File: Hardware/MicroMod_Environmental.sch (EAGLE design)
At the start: 26 parts, among them J1 MICROMOD_STANDARD, U1 SGP40, U3 SHTC3, U4 3.3V, U5 STC31

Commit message: Routed
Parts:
- added U2: EEPROM, SparkFun-IC-Memory:EEPROM-I2C512K
- C5, C6: device SparkFun-Capacitors:1.0UF-0402T-16V-10% -> SparkFun-Capacitors:1.0UF-0603-16V-10%
- R12: value 100K -> 100k; device SparkFun-Resistors:100KOHM-0402-1/16W-1% -> SparkFun-Resistors:100KOHM-0603-1/10W-1%
- R3: device SparkFun-Resistors:1KOHM-0402T-1/16W-1% -> SparkFun-Resistors:1KOHM-0603-1/10W-1%
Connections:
- removed net GND1: LED2.C
- new net A0: J1.EEPROM_A0, U2.A0
- new net A1: J1.EEPROM_A1, U2.A1
- new net A2: J1.EEPROM_A2, U2.A2
- net 3.3V: now also U2.VCC; no longer J1.3.3V
- net GND: now also LED2.C, U2.GND, U2.WP
- net SCL: now also U2.SCL
- net SDA: now also U2.SDA
- net VCC: now also J1.VCC
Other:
- note added: "EEPROM"
- moved on the sheet: 0X2A, 0X2B, 0X2C, C2, C3, C4, C5, C6, C7, J1, JP1, LED2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

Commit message: Small tweaks to traces
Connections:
- removed net 3.3V1: PWR\.2
- net 3.3V: now also PWR\.2
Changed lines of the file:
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@@
 <wire x1="68.58" y1="76.2" x2="68.58" y2="78.74" width="0.1524" layer="91"/>
+</segment>
+<segment>
+<wire x1="142.24" y1="190.5" x2="139.7" y2="190.5" width="0.1524" layer="91"/>
+<pinref part="PWR\" gate="G$1" pin="2"/>
+<pinref part="SUPPLY12" gate="G$1" pin="3.3V"/>
+<wire x1="139.7" y1="190.5" x2="139.7" y2="200.66" width="0.1524" layer="91"/>
 </segment>
 </net>
@@
 </segment>
 </net>
-<net name="3.3V1" class="2">
-<segment>
-<wire x1="142.24" y1="190.5" x2="139.7" y2="190.5" width="0.1524" layer="91"/>
-<wire x1="139.7" y1="200.66" x2="139.7" y2="190.5" width="0.1524" layer="91"/>
-<pinref part="PWR\" gate="G$1" pin="2"/>
-<pinref part="SUPPLY12" gate="G$1" pin="3.3V"/>
-</segment>
-</net>

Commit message: Adds silk, fiducials, and version number
* Adds text to part boxes in schematic
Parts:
- added FD1, FD2, FD3, FD4: FIDUCIAL1X2, SparkFun-Aesthetics:FIDUCIAL1X2
- added LOGO1: SFE_LOGO_NAME_FLAME.2_INCH, SparkFun-Aesthetics:SFE_LOGO_NAME_FLAME.2_INCH
- added LOGO2: OSHW-LOGOS, SparkFun-Aesthetics:OSHW-LOGOS
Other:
- note added: "Air Quality Sensor: SGP40"
- note added: "CO2 Sensor: STC31"
- note added: "Function Connector"
- note added: "Humidity and Temperature: SHTC3"
- note added: "Jumpers"
- note added: "Voltage Regulation"
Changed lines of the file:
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@@
 <part name="SUPPLY13" library="SparkFun-PowerSymbols" deviceset="VCC" device=""/>
 <part name="GND10" library="SparkFun-PowerSymbols" deviceset="GND" device=""/>
+<part name="LOGO1" library="SparkFun-Aesthetics" deviceset="SFE_LOGO_NAME_FLAME" device=".2_INCH" value="SFE_LOGO_NAME_FLAME.2_INCH"/>
+<part name="LOGO2" library="SparkFun-Aesthetics" deviceset="OSHW-LOGO" device="S"/>
+<part name="FD1" library="SparkFun-Aesthetics" deviceset="FIDUCIAL" device="1X2"/>
+<part name="FD2" library="SparkFun-Aesthetics" deviceset="FIDUCIAL" device="1X2"/>
+<part name="FD3" library="SparkFun-Aesthetics" deviceset="FIDUCIAL" device="1X2"/>
+<part name="FD4" library="SparkFun-Aesthetics" deviceset="FIDUCIAL" device="1X2"/>
 </parts>
 <sheets>
@@
 <wire x1="111.76" y1="160.02" x2="223.52" y2="160.02" width="0.1524" layer="97" style="longdash"/>
 <wire x1="111.76" y1="279.4" x2="111.76" y2="160.02" width="0.1524" layer="97" style="longdash"/>
+<text x="38.1" y="269.24" size="2.54" layer="94" font="vector">Voltage Regulation</text>
+<text x="154.94" y="271.78" size="2.54" layer="94" font="vector">Jumpers</text>
+<text x="297.18" y="271.78" size="2.54" layer="94" font="vector">Humidity and Temperature: SHTC3</text>
+<text x="309.88" y="195.58" size="2.54" layer="94" font="vector">CO2 Sensor: STC31</text>
+<text x="96.52" y="149.86" size="2.54" layer="94" font="vector">Function Connector</text>
+<text x="309.88" y="109.22" size="2.54" layer="94" font="vector">Air Quality Sensor: SGP40</text>
 </plain>
 <instances>
@@
 <attribute name="VALUE" x="180.34" y="182.88" size="1.778" layer="96" font="vector"/>
 </instance>
+<instance part="LOGO1" gate="G$1" x="330.2" y="35.56" smashed="yes"/>
+<instance part="LOGO2" gate="G$1" x="401.32" y="48.26" smashed="yes"/>
+<instance part="FD1" gate="G$1" x="421.64" y="33.02" smashed="yes"/>
+<instance part="FD2" gate="G$1" x="419.1" y="30.48" smashed="yes"/>
+<instance part="FD3" gate="G$1" x="419.1" y="33.02" smashed="yes"/>
+<instance part="FD4" gate="G$1" x="421.64" y="30.48" smashed="yes"/>
 </instances>
 <busses>

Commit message: Reroutes board
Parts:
- renumbered LED2 to LED1
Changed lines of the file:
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@@
 <part name="SUPPLY7" library="SparkFun-PowerSymbols" deviceset="VCC" device=""/>
 <part name="R3" library="SparkFun-Resistors" deviceset="1KOHM" device="-0603-1/10W-1%" value="1k"/>
-<part name="LED2" library="SparkFun-LED" deviceset="LED-RED" device="0603" value="RED"/>
+<part name="LED1" library="SparkFun-LED" deviceset="LED-RED" device="0603" value="RED"/>
 <part name="PWR\" library="SparkFun-Jumpers" deviceset="JUMPER-SMT_2_NC_TRACE" device="_SILK" package3d_urn="urn:adsk.eagle:package:39281/1" value="JUMPER-SMT_2_NC_TRACE_SILK"/>
 <part name="SUPPLY12" library="SparkFun-PowerSymbols" deviceset="3.3V" device=""/>
@@
 <attribute name="VALUE" x="155.448" y="191.008" size="1.778" layer="96" font="vector" rot="R180" align="top-center"/>
 </instance>
-<instance part="LED2" gate="G$1" x="170.18" y="190.5" smashed="yes" rot="R90">
+<instance part="LED1" gate="G$1" x="170.18" y="190.5" smashed="yes" rot="R90">
 <attribute name="NAME" x="179.832" y="190.119" size="1.778" layer="95" font="vector" rot="R180"/>
 <attribute name="VALUE" x="178.308" y="191.008" size="1.778" layer="96" font="vector" rot="R180" align="top-left"/>
@@
 <wire x1="182.88" y1="190.5" x2="175.26" y2="190.5" width="0.1524" layer="91"/>
 <wire x1="182.88" y1="190.5" x2="182.88" y2="187.96" width="0.1524" layer="91"/>
-<pinref part="LED2" gate="G$1" pin="C"/>
+<pinref part="LED1" gate="G$1" pin="C"/>
 <pinref part="GND10" gate="1" pin="GND"/>
 </segment>
@@
 <wire x1="167.64" y1="190.5" x2="165.1" y2="190.5" width="0.1524" layer="91"/>
 <pinref part="R3" gate="G$1" pin="1"/>
-<pinref part="LED2" gate="G$1" pin="A"/>
+<pinref part="LED1" gate="G$1" pin="A"/>
 </segment>
 </net>

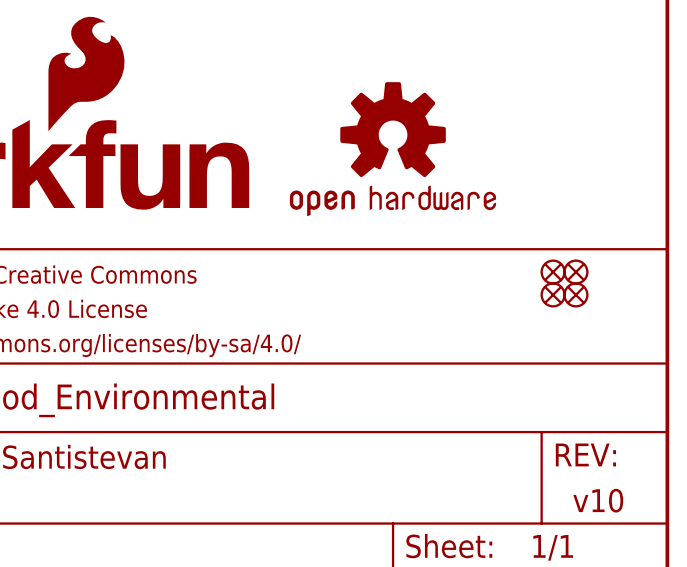
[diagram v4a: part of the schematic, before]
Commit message: Adds address table in silk, adds a more symmetrical cutout around IC's, labels ICs in silk
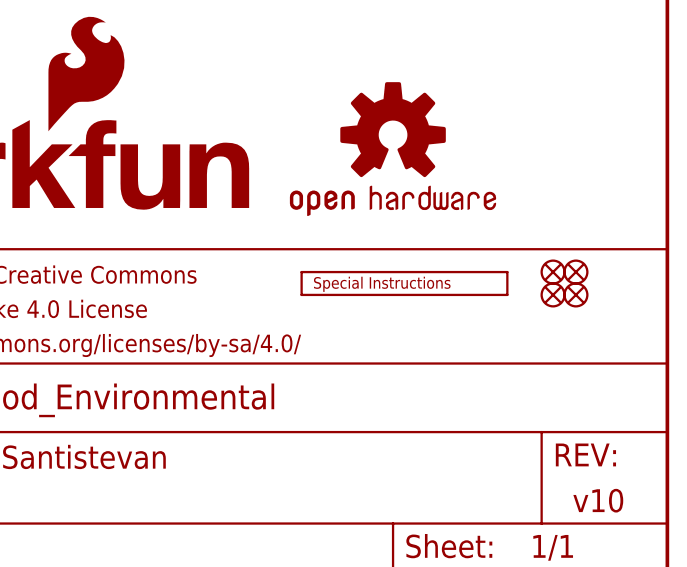
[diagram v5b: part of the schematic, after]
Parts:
- added LOGO3: SPECIAL_INSTRUCTIONS-ORDERING, SparkFun-Aesthetics:SPECIAL_INSTRUCTIONS-ORDERING
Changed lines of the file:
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@@
 <part name="FD3" library="SparkFun-Aesthetics" deviceset="FIDUCIAL" device="1X2"/>
 <part name="FD4" library="SparkFun-Aesthetics" deviceset="FIDUCIAL" device="1X2"/>
+<part name="LOGO3" library="SparkFun-Aesthetics" deviceset="SPECIAL_INSTRUCTIONS" device="-ORDERING"/>
 </parts>
 <sheets>
@@
 <instance part="FD3" gate="G$1" x="419.1" y="33.02" smashed="yes"/>
 <instance part="FD4" gate="G$1" x="421.64" y="30.48" smashed="yes"/>
+<instance part="LOGO3" gate="G$1" x="391.16" y="30.48" smashed="yes"/>
 </instances>
 <busses>

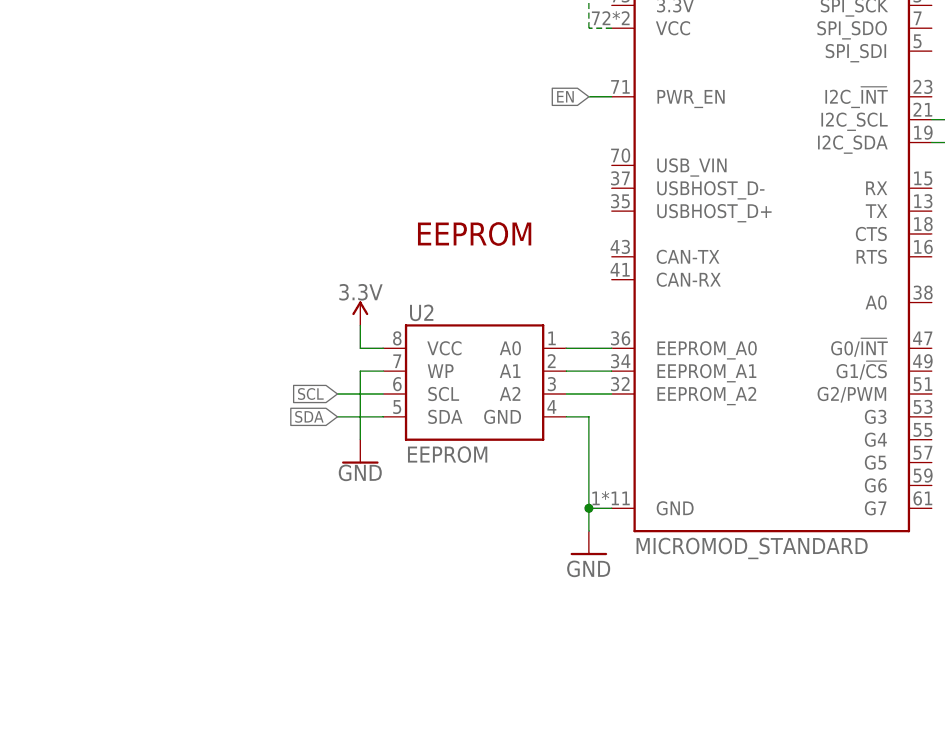
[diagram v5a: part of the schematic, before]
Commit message: Adds pullup and jumper to the EEPROM's write protect, brings WP pin to card's edge
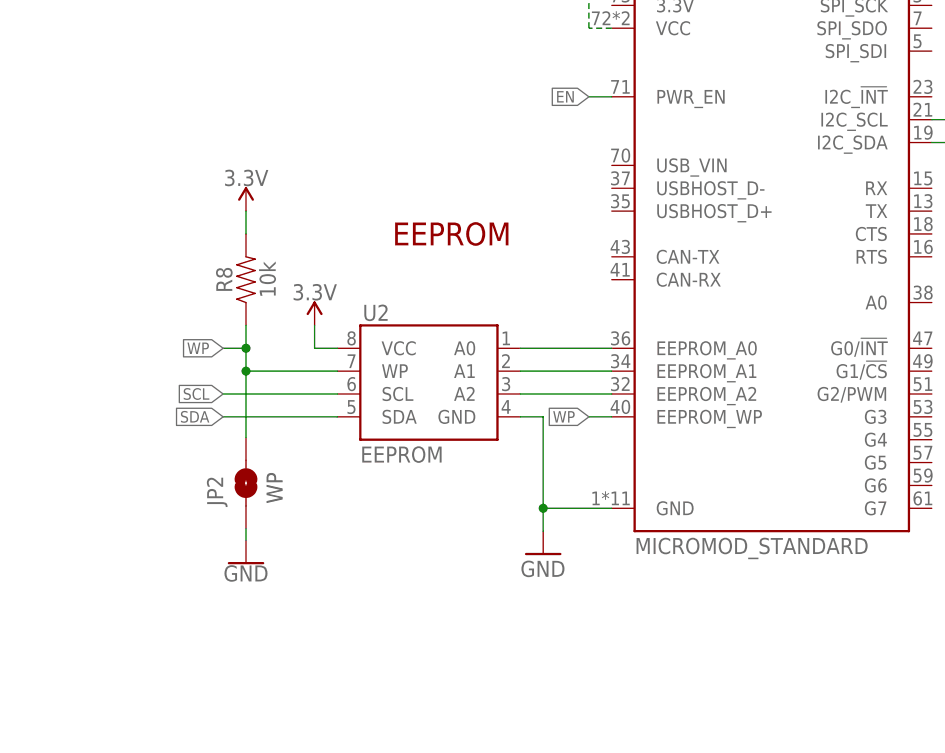
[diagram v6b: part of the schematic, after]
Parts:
- added JP2: JUMPER-SMT_2_NO_SILK, SparkFun-Jumpers:JUMPER-SMT_2_NO_SILK
- added R8: 10k, SparkFun-Resistors:10KOHM-0603-1/10W-1%
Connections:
- new net WP: J1.EEPROM_WP, JP2.2, R8.1, U2.WP
- net 3.3V: now also R8.2
- net GND: now also JP2.1; no longer U2.WP
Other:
- note added: "WP"
- moved on the sheet: U2
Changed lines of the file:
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@@
 <part name="FD4" library="SparkFun-Aesthetics" deviceset="FIDUCIAL" device="1X2"/>
 <part name="LOGO3" library="SparkFun-Aesthetics" deviceset="SPECIAL_INSTRUCTIONS" device="-ORDERING"/>
+<part name="SUPPLY15" library="SparkFun-PowerSymbols" deviceset="3.3V" device=""/>
+<part name="R8" library="SparkFun-Resistors" deviceset="10KOHM" device="-0603-1/10W-1%" value="10k"/>
+<part name="JP2" library="SparkFun-Jumpers" deviceset="JUMPER-SMT_2_NO" device="_SILK" package3d_urn="urn:adsk.eagle:package:39279/1"/>
 </parts>
 <sheets>
@@
 <text x="297.18" y="53.34" size="1.778" layer="97" font="vector" align="center">Abs min/max Vdd and Vddh: -0.3 to +3.6V
 Operating current @ 3.3V: 3.0 mA</text>
-<text x="81.28" y="88.9" size="2.54" layer="94" font="vector" align="center">EEPROM</text>
+<text x="78.74" y="88.9" size="2.54" layer="94" font="vector" align="center">EEPROM</text>
 <wire x1="223.52" y1="279.4" x2="223.52" y2="205.74" width="0.1524" layer="97" style="longdash"/>
 <wire x1="223.52" y1="205.74" x2="223.52" y2="160.02" width="0.1524" layer="97" style="longdash"/>
@@
 <text x="96.52" y="149.86" size="2.54" layer="94" font="vector">Function Connector</text>
 <text x="309.88" y="109.22" size="2.54" layer="94" font="vector">Air Quality Sensor: SGP40</text>
+<text x="59.944" y="58.928" size="1.778" layer="97" font="vector" rot="R90">WP</text>
 </plain>
 <instances>
@@
 <attribute name="NAME" x="157.226" y="243.205" size="1.778" layer="95" font="vector"/>
 </instance>
-<instance part="GND8" gate="1" x="93.98" y="53.34" smashed="yes">
-<attribute name="VALUE" x="91.44" y="50.8" size="1.778" layer="96" font="vector"/>
-</instance>
-<instance part="U2" gate="G$1" x="81.28" y="71.12" smashed="yes" rot="MR0">
-<attribute name="NAME" x="73.914" y="79.248" size="1.778" layer="95"/>
-<attribute name="VALUE" x="73.66" y="63.5" size="1.778" layer="96"/>
-</instance>
-<instance part="SUPPLY14" gate="G$1" x="68.58" y="78.74" smashed="yes">
-<attribute name="VALUE" x="68.58" y="81.534" size="1.778" layer="96" align="bottom-center"/>
-</instance>
-<instance part="GND9" gate="1" x="68.58" y="63.5" smashed="yes">
-<attribute name="VALUE" x="68.58" y="63.246" size="1.778" layer="96" align="top-center"/>
+<instance part="GND8" gate="1" x="88.9" y="53.34" smashed="yes">
+<attribute name="VALUE" x="86.36" y="50.8" size="1.778" layer="96" font="vector"/>
+</instance>
+<instance part="U2" gate="G$1" x="76.2" y="71.12" smashed="yes" rot="MR0">
+<attribute name="NAME" x="68.834" y="79.248" size="1.778" layer="95"/>
+<attribute name="VALUE" x="68.58" y="63.5" size="1.778" layer="96"/>
+</instance>
+<instance part="SUPPLY14" gate="G$1" x="63.5" y="78.74" smashed="yes">
+<attribute name="VALUE" x="63.5" y="81.534" size="1.778" layer="96" align="bottom-center"/>
+</instance>
+<instance part="GND9" gate="1" x="55.88" y="52.324" smashed="yes">
+<attribute name="VALUE" x="55.88" y="52.07" size="1.778" layer="96" align="top-center"/>
 </instance>
 <instance part="SUPPLY13" gate="G$1" x="93.98" y="116.84" smashed="yes">
@@
 <instance part="FD4" gate="G$1" x="421.64" y="30.48" smashed="yes"/>
 <instance part="LOGO3" gate="G$1" x="391.16" y="30.48" smashed="yes"/>
+<instance part="SUPPLY15" gate="G$1" x="55.88" y="91.44" smashed="yes">
+<attribute name="VALUE" x="55.88" y="94.234" size="1.778" layer="96" align="bottom-center"/>
+</instance>
+<instance part="R8" gate="G$1" x="55.88" y="83.82" smashed="yes" rot="R90">
+<attribute name="NAME" x="54.356" y="83.82" size="1.778" layer="95" font="vector" rot="R90" align="bottom-center"/>
+<attribute name="VALUE" x="57.404" y="83.82" size="1.778" layer="96" font="vector" rot="R90" align="top-center"/>
+</instance>
+<instance part="JP2" gate="G$1" x="55.88" y="61.214" smashed="yes" rot="R90">
+<attribute name="NAME" x="53.34" y="58.674" size="1.778" layer="95" font="vector" rot="R90"/>
+</instance>
 </instances>
 <busses>
@@
 <segment>
 <pinref part="U2" gate="G$1" pin="VCC"/>
-<wire x1="71.12" y1="76.2" x2="68.58" y2="76.2" width="0.1524" layer="91"/>
+<wire x1="66.04" y1="76.2" x2="63.5" y2="76.2" width="0.1524" layer="91"/>
 <pinref part="SUPPLY14" gate="G$1" pin="3.3V"/>
-<wire x1="68.58" y1="76.2" x2="68.58" y2="78.74" width="0.1524" layer="91"/>
+<wire x1="63.5" y1="76.2" x2="63.5" y2="78.74" width="0.1524" layer="91"/>
 </segment>
 <segment>
@@
 <pinref part="SUPPLY12" gate="G$1" pin="3.3V"/>
 <wire x1="139.7" y1="190.5" x2="139.7" y2="200.66" width="0.1524" layer="91"/>
+</segment>
+<segment>
+<pinref part="R8" gate="G$1" pin="2"/>
+<pinref part="SUPPLY15" gate="G$1" pin="3.3V"/>
+<wire x1="55.88" y1="88.9" x2="55.88" y2="91.44" width="0.1524" layer="91"/>
 </segment>
 </net>
@@
 <segment>
 <pinref part="J1" gate="J1" pin="GND"/>
-<wire x1="96.52" y1="58.42" x2="93.98" y2="58.42" width="0.1524" layer="91"/>
-<wire x1="93.98" y1="58.42" x2="93.98" y2="55.88" width="0.1524" layer="91"/>
+<wire x1="96.52" y1="58.42" x2="88.9" y2="58.42" width="0.1524" layer="91"/>
+<wire x1="88.9" y1="58.42" x2="88.9" y2="55.88" width="0.1524" layer="91"/>
 <pinref part="GND8" gate="1" pin="GND"/>
 <pinref part="U2" gate="G$1" pin="GND"/>
-<wire x1="91.44" y1="68.58" x2="93.98" y2="68.58" width="0.1524" layer="91"/>
-<wire x1="93.98" y1="68.58" x2="93.98" y2="58.42" width="0.1524" layer="91"/>
-<junction x="93.98" y="58.42"/>
-</segment>
-<segment>
-<pinref part="U2" gate="G$1" pin="WP"/>
-<wire x1="71.12" y1="73.66" x2="68.58" y2="73.66" width="0.1524" layer="91"/>
-<wire x1="68.58" y1="73.66" x2="68.58" y2="66.04" width="0.1524" layer="91"/>
-<pinref part="GND9" gate="1" pin="GND"/>
+<wire x1="86.36" y1="68.58" x2="88.9" y2="68.58" width="0.1524" layer="91"/>
+<wire x1="88.9" y1="68.58" x2="88.9" y2="58.42" width="0.1524" layer="91"/>
+<junction x="88.9" y="58.42"/>
 </segment>
 <segment>
@@
 <pinref part="LED1" gate="G$1" pin="C"/>
 <pinref part="GND10" gate="1" pin="GND"/>
+</segment>
+<segment>
+<pinref part="JP2" gate="G$1" pin="1"/>
+<pinref part="GND9" gate="1" pin="GND"/>
+<wire x1="55.88" y1="56.134" x2="55.88" y2="54.864" width="0.1524" layer="91"/>
 </segment>
 </net>
@@
 <segment>
 <pinref part="U2" gate="G$1" pin="SCL"/>
-<wire x1="71.12" y1="71.12" x2="66.04" y2="71.12" width="0.1524" layer="91"/>
-<label x="66.04" y="71.12" size="1.27" layer="95" rot="R180" xref="yes"/>
+<wire x1="66.04" y1="71.12" x2="53.34" y2="71.12" width="0.1524" layer="91"/>
+<label x="53.34" y="71.12" size="1.27" layer="95" rot="R180" xref="yes"/>
 </segment>
 </net>
@@
 <segment>
 <pinref part="U2" gate="G$1" pin="SDA"/>
-<wire x1="71.12" y1="68.58" x2="66.04" y2="68.58" width="0.1524" layer="91"/>
-<label x="66.04" y="68.58" size="1.27" layer="95" rot="R180" xref="yes"/>
+<wire x1="66.04" y1="68.58" x2="53.34" y2="68.58" width="0.1524" layer="91"/>
+<label x="53.34" y="68.58" size="1.27" layer="95" rot="R180" xref="yes"/>
 </segment>
 </net>
@@
 <segment>
 <pinref part="U2" gate="G$1" pin="A0"/>
-<wire x1="91.44" y1="76.2" x2="96.52" y2="76.2" width="0.1524" layer="91"/>
+<wire x1="86.36" y1="76.2" x2="96.52" y2="76.2" width="0.1524" layer="91"/>
 <pinref part="J1" gate="J1" pin="EEPROM_A0"/>
 </segment>
@@
 <segment>
 <pinref part="U2" gate="G$1" pin="A2"/>
-<wire x1="91.44" y1="71.12" x2="96.52" y2="71.12" width="0.1524" layer="91"/>
+<wire x1="86.36" y1="71.12" x2="96.52" y2="71.12" width="0.1524" layer="91"/>
 <pinref part="J1" gate="J1" pin="EEPROM_A2"/>
 </segment>
@@
 <segment>
 <pinref part="U2" gate="G$1" pin="A1"/>
-<wire x1="91.44" y1="73.66" x2="96.52" y2="73.66" width="0.1524" layer="91"/>
+<wire x1="86.36" y1="73.66" x2="96.52" y2="73.66" width="0.1524" layer="91"/>
 <pinref part="J1" gate="J1" pin="EEPROM_A1"/>
 </segment>
 </net>
+<net name="WP" class="0">
+<segment>
+<pinref part="J1" gate="J1" pin="EEPROM_WP"/>
+<wire x1="96.52" y1="68.58" x2="93.98" y2="68.58" width="0.1524" layer="91"/>
+<label x="93.98" y="68.58" size="1.27" layer="95" rot="R180" xref="yes"/>
+</segment>
+<segment>
+<pinref part="U2" gate="G$1" pin="WP"/>
+<wire x1="66.04" y1="73.66" x2="55.88" y2="73.66" width="0.1524" layer="91"/>
+<pinref part="R8" gate="G$1" pin="1"/>
+<wire x1="55.88" y1="76.2" x2="55.88" y2="73.66" width="0.1524" layer="91"/>
+<wire x1="55.88" y1="76.2" x2="55.88" y2="78.74" width="0.1524" layer="91"/>
+<wire x1="53.34" y1="76.2" x2="55.88" y2="76.2" width="0.1524" layer="91"/>
+<junction x="55.88" y="76.2"/>
+<pinref part="JP2" gate="G$1" pin="2"/>
+<wire x1="55.88" y1="73.66" x2="55.88" y2="66.294" width="0.1524" layer="91"/>
+<junction x="55.88" y="73.66"/>
+<label x="53.34" y="76.2" size="1.27" layer="95" rot="R180" xref="yes"/>
+</segment>
+</net>
